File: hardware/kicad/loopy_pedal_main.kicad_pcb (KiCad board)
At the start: 2 copper layers, 94 x 86 mm, 76 parts, among them J1 USB_C_Receptacle_USB2.0_16P, J10 Conn_01x02, J11 Conn_01x03, J2 Barrel_Jack, J3 Conn_01x06, J4 Conn_01x06, J5 Conn_01x08, J6 Conn_02x03_Odd_Even, J7 Conn_02x03_Odd_Even, J8 DIN-5_180degree, J9 DIN-5_180degree, Q1 AO3401A, SW1 SW_Push, SW2 SW_Push, U1 ATmega328P-A, U10 74AHCT1G08, U2 ATmega16U2-A, U3 AP63203WU, U4 74AHCT1G125, U5 LM66100DCK, U6 LM66100DCK, U7 USBLC6-2SC6, U8 74AHCT1G125, U9 H11L1, Y1 16MHz, Y2 16MHz

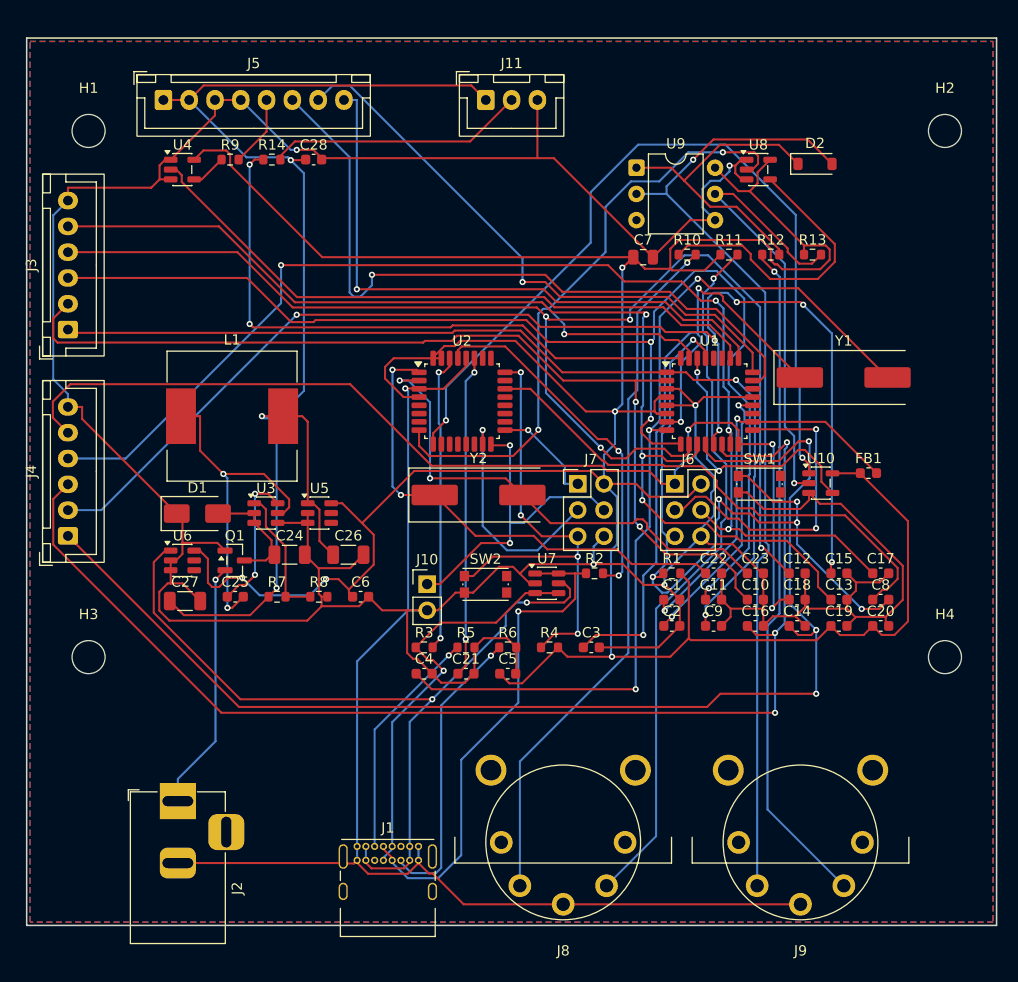
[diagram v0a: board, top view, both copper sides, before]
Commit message: fix(pcb): correct right-angle MIDI DIN footprint + 3D model, tighter Y
The previous DIN footprint used the vertical-mount contact-circle pattern on a
right-angle body (wrong orientation). Replaced with the genuine right-angle
landing pattern (pins 1/2/3 in a column, 4/5 offset) sourced from
schilkp/KiCad_Devices (MIT), with shield/mounting posts 15mm apart + ground
tabs. Rebuilt the 3D body to match (shielded box + square flange + recessed
round socket + pins), oriented so the socket faces out the edge.

Because the corrected jack is ~16mm deep (vs ~21mm), pulled the board in on Y:
94x79mm (was 94x86). Re-routed clean: 905 segments / 74 vias, 0 DRC / 0 unrouted.
Gerbers + doc updated.

Co-Authored-By: Claude Opus 4.8 <noreply@anthropic.com>
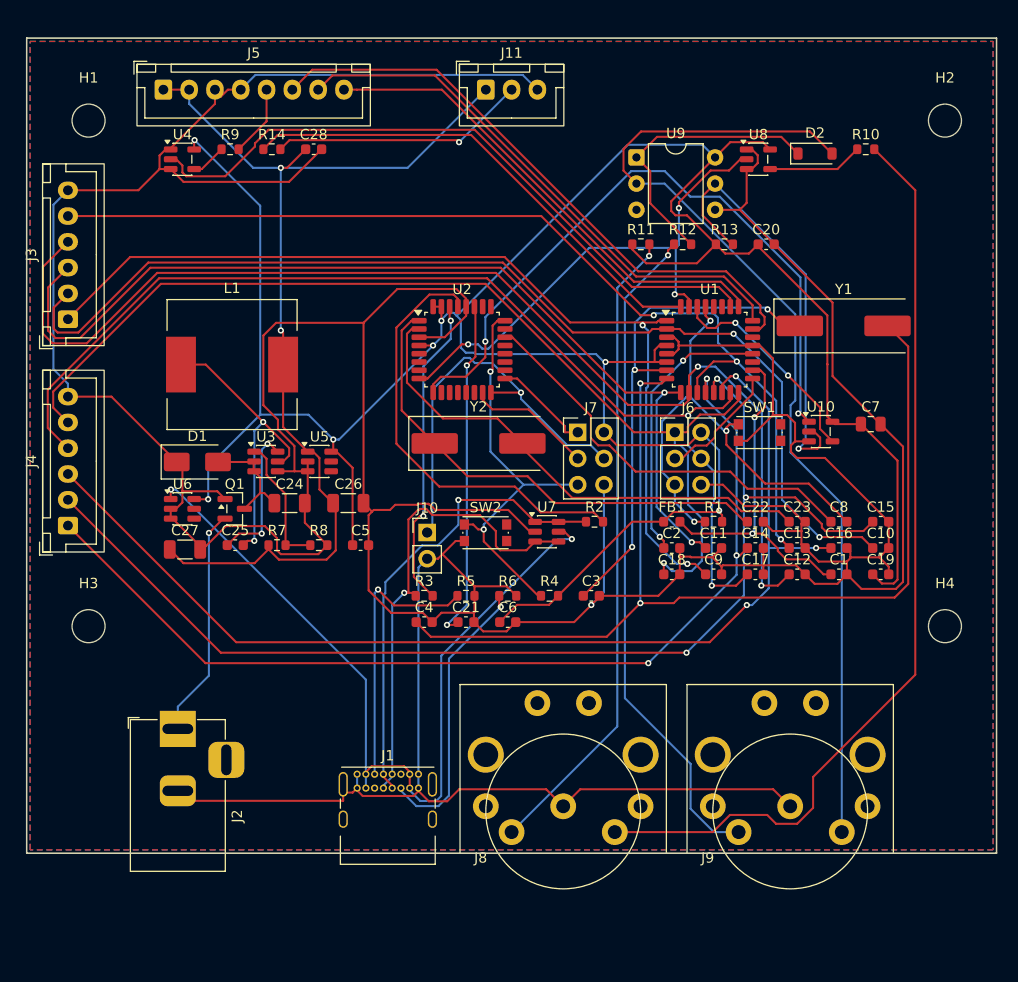
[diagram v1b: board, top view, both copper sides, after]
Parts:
- moved C20 38.6 mm to (101.7, 50.0)
- moved C7 27.4 mm to (111.8, 67.4)
- moved R10 20.1 mm to (111.3, 40.8)
- moved FB1 19.6 mm to (92.5, 76.9)
- moved C5 18.9 mm to (62.4, 79.1)
- moved C1 16.4 mm to (108.7, 82.0)
- moved C6 14.5 mm to (76.6, 86.6)
- moved C10 13.1 mm to (112.8, 79.4)
- moved C18 12.4 mm to (92.5, 82.0)
- moved C17 12.2 mm to (100.6, 82.0)
- moved C16 11.1 mm to (108.7, 79.4)
- moved R13 8.60 mm to (97.6, 50.0)
- moved R11 8.60 mm to (89.5, 50.0)
- moved R12 8.60 mm to (93.6, 50.0)
- moved C8 8.57 mm to (108.7, 76.9)
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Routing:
- net GND: track 494.4 -> 547.1 mm, vias 6 -> 1
- net +5V: track 317.3 -> 270.2 mm, vias 5 -> 7
- net RST_328: track 74.1 -> 48.1 mm, vias 6 -> 3
- net SW_UNDO: track 119.7 -> 94.2 mm, vias 3 -> 2
- net UART_TX: track 75.0 -> 50.2 mm
- net SW_TRACK2: track 121.4 -> 96.8 mm
- net N$17: track 68.2 -> 90.5 mm, vias 1 -> 0
- net +5V_LED: track 121.7 -> 99.5 mm, vias 3 -> 2
- net N$5: track 31.4 -> 11.9 mm, vias 2 -> 0
- net MIDI_OUT_BUF: track 28.4 -> 9.24 mm
- net N$3: track 67.1 -> 49.0 mm
- net SW_MODE: track 127.6 -> 112.8 mm, vias 4 -> 2
- net M16_TXD: track 80.9 -> 66.2 mm
- net SW_TRACK4: track 120.7 -> 107.2 mm
- net ENC_SW: track 60.0 -> 47.4 mm, vias 1 -> 0
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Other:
- board size 94 x 86 mm -> 94 x 79 mm

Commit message: refactor(pcb): compact wide-short layout, 80x66mm (was 94x79)
Re-floorplanned to a dense wide-and-short shape to kill the ~60% dead space:
external I/O (barrel, USB-C, both MIDI DIN) along the bottom edge, internal
headers (ring, indicator, 2x footswitch) along the top, and the logic packed
into a 4-column band between them. Generalized the edge-placement helper to any
edge. 29% smaller area, re-routed clean: 911 segments / 74 vias, 0 DRC / 0 unrouted.

Co-Authored-By: Claude Opus 4.8 <noreply@anthropic.com>
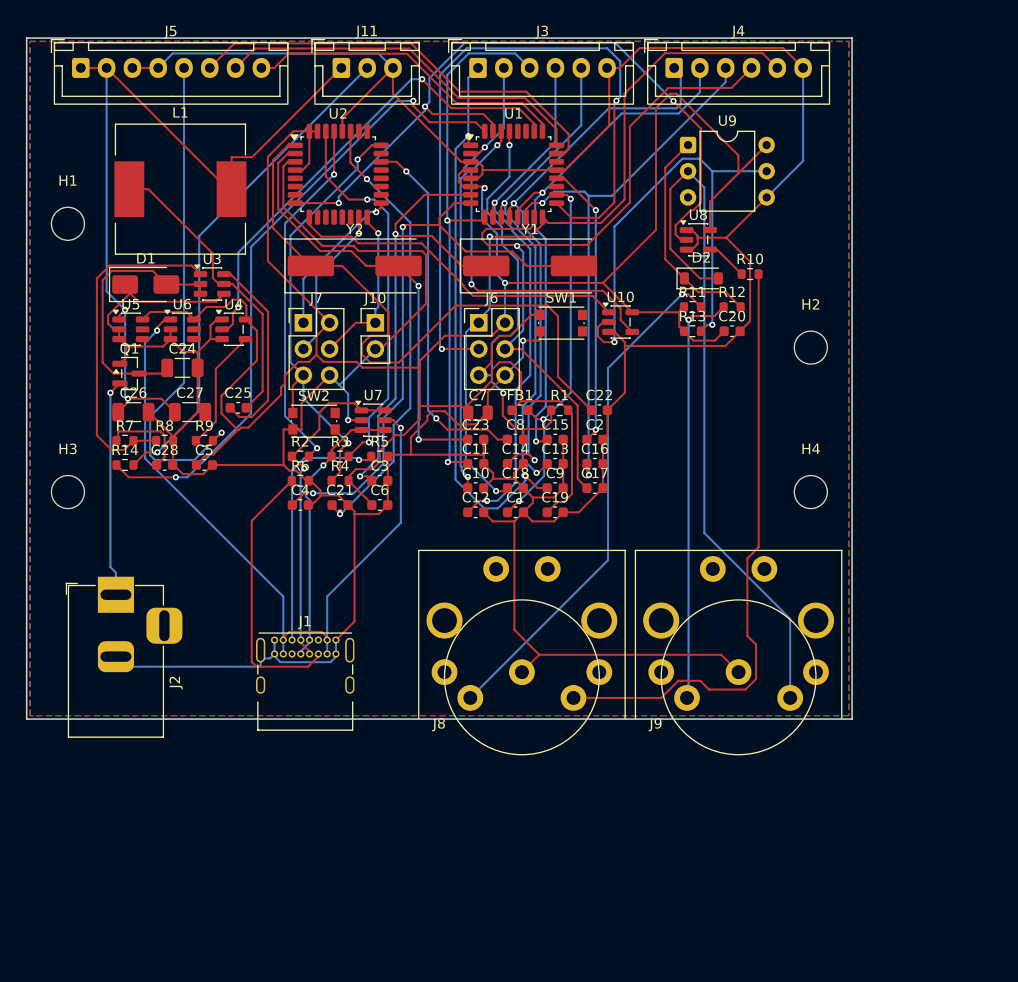
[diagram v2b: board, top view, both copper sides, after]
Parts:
- moved J4 73.6 mm to (92.8, 32.9), turned to 0 degrees
- moved J3 46.6 mm to (73.8, 32.9), turned to 0 degrees
- moved C10 39.7 mm to (73.5, 73.6)
- moved C7 38.1 mm to (73.7, 66.3)
- moved C28 33.8 mm to (43.4, 71.4)
- moved R14 33.8 mm to (39.5, 71.4)
- moved C15 32.5 mm to (81.2, 68.9)
- moved C8 32.3 mm to (77.4, 68.9)
- moved C23 32.2 mm to (73.5, 68.9)
- moved C19 32.1 mm to (81.2, 76.0)
- moved C1 31.9 mm to (77.4, 76.0)
- moved C12 31.7 mm to (73.5, 76.0)
- moved Y1 30.9 mm to (78.8, 52.1)
- moved R2 29.2 mm to (56.5, 70.6)
- moved J7 28.6 mm to (56.8, 57.6)
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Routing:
- net GND: track 547.1 -> 435.9 mm, vias 1 -> 2
- net SW_MODE: track 112.8 -> 52.0 mm
- net SW_STOP: track 104.7 -> 44.5 mm
- net SW_TRACK3: track 111.9 -> 51.8 mm, vias 3 -> 2
- net N$5: track 11.9 -> 70.0 mm, vias 0 -> 2
- net SW_TRACK4: track 107.2 -> 55.2 mm, vias 3 -> 2
- net SW_TRACK1: track 98.3 -> 47.5 mm, vias 3 -> 2
- net N$4: track 100.3 -> 56.8 mm
- net SW_TRACK2: track 96.8 -> 55.4 mm, vias 3 -> 2
- net RING_DATA_OUT: track 6.90 -> 48.3 mm, vias 0 -> 1
- net SW_UNDO: track 94.2 -> 52.9 mm
- net SW_RECPLAY: track 91.4 -> 53.9 mm
- net +5V: track 270.2 -> 236.0 mm, vias 7 -> 2
- net M16_TXD: track 66.2 -> 33.3 mm, vias 2 -> 0
- net SW_CLEAR: track 105.5 -> 73.2 mm, vias 2 -> 1
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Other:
- board size 94 x 79 mm -> 80 x 66 mm
